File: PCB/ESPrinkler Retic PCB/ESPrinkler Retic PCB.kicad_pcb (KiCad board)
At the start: 2 copper layers, 120.4 x 85.7 mm, 138 parts, among them J4 Conn_01x19, J5 Conn_01x19, J6 Conn_01x04, Q1 AO3400A, Q10 AO3400A, Q11 AO3400A, Q2 AO3400A, Q3 AO3400A, Q4 AO3400A, Q5 AO3400A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

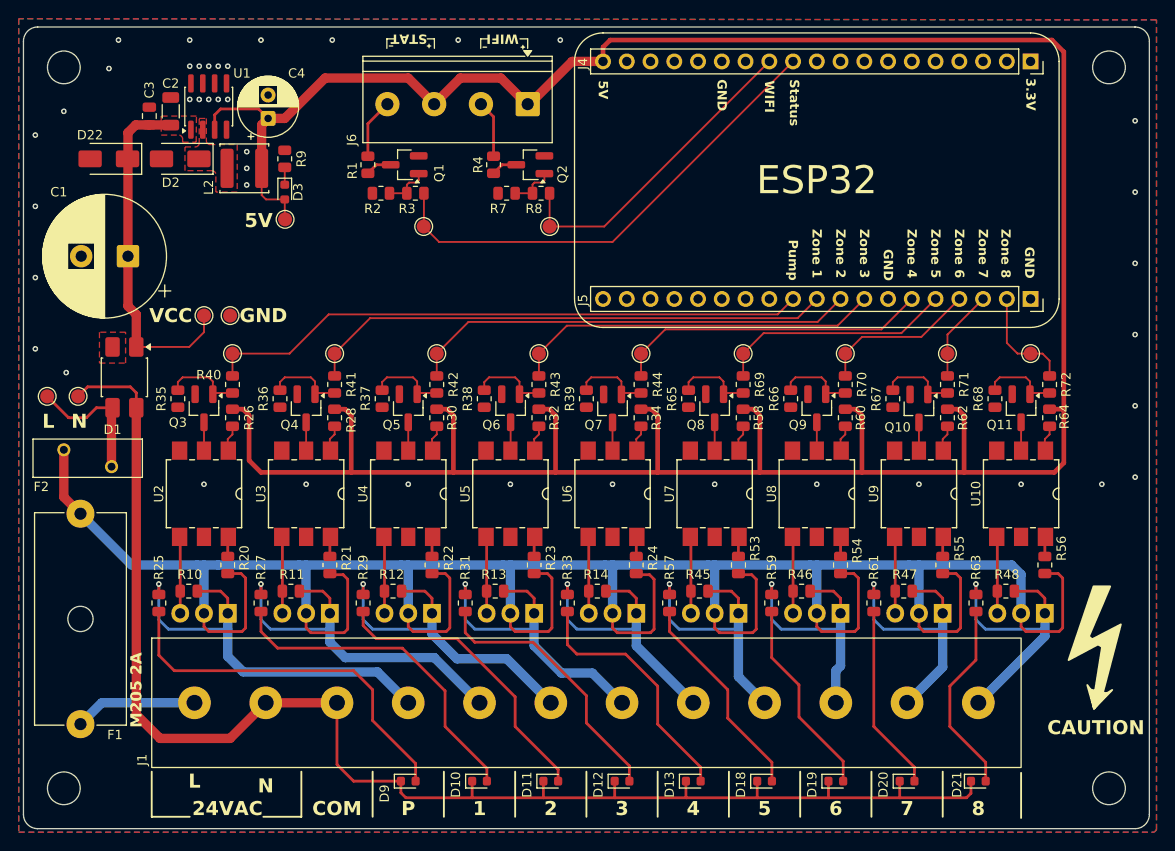
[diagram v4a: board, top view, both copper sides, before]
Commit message: Labelling as V2.0
Repo needs to change, I have been using it poorly. V2.0 will be the next "main branch". After that, forks will be used instead

Also in this commit, I have updated the custom footprints and updated the links to them in the project.
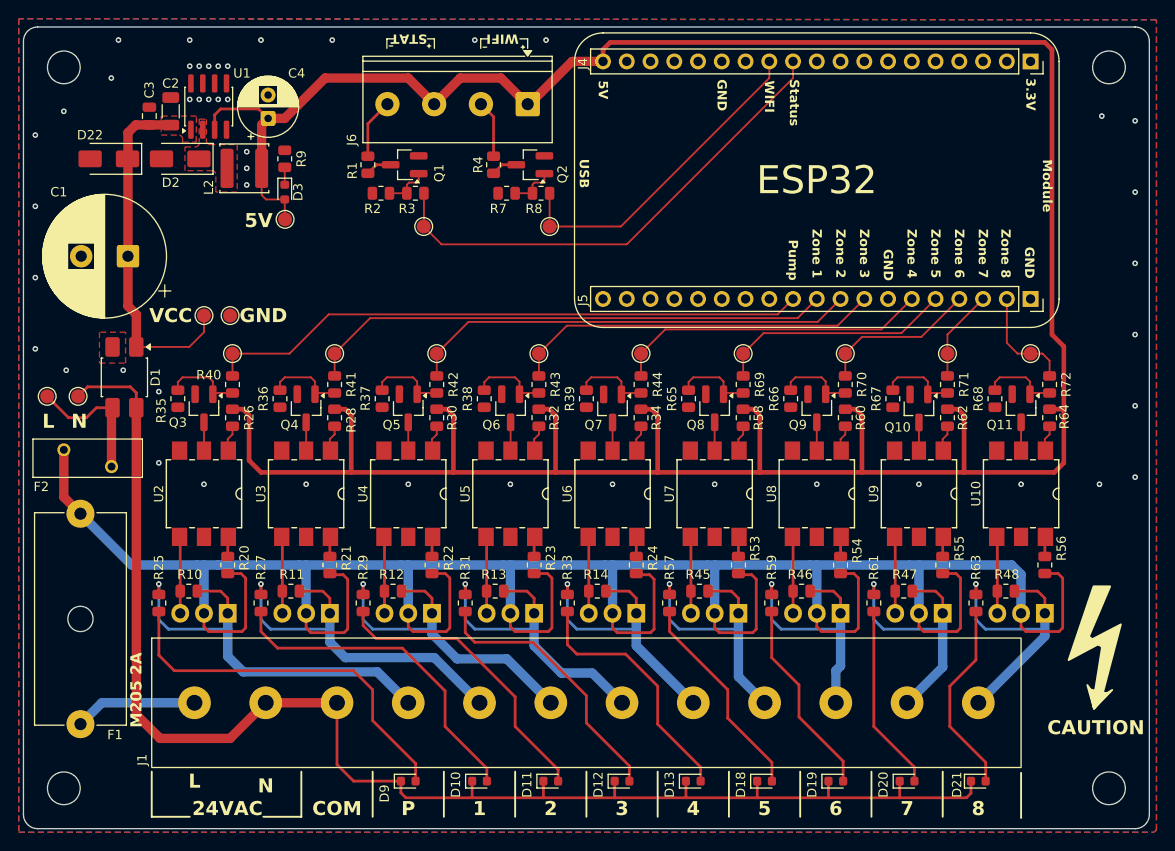
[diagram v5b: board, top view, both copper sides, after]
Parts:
- C4: value 220uF -> 180uF
- D1: footprint Package_SO:OnSemi_751EP_SOIC-4_3.9x4.725mm_P2.54mm -> Footprints:OnSemi_751EP_SOIC-4_3.9x4.725mm_P2.54mm
- D14, D15, D16, D17, D4, D5, D6, D7, D8: value Generic_Triac_A1A2G -> BTB16-600BWRG
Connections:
- net /ESP32/Pump renamed /Control Outputs/Pump Input
- net /ESP32/Status LED renamed /ESP32/Status LED CTRL
- net /ESP32/WIFI LED renamed /ESP32/WIFI LED CTRL
- net /ESP32/Zone 1 renamed /Control Outputs/Zone 1 Input
- net /ESP32/Zone 2 renamed /Control Outputs/Zone 2 Input
- net /ESP32/Zone 3 renamed /Control Outputs/Zone 3 Input
- net /ESP32/Zone 4 renamed /Control Outputs/Zone 4 Input
- net /ESP32/Zone 5 renamed /Control Outputs/Zone 5 Input
- net /ESP32/Zone 6 renamed /Control Outputs/Zone 6 Input
- net /ESP32/Zone 7 renamed /Control Outputs/Zone 7 Input
- net /ESP32/Zone 8 renamed /Control Outputs/Zone 8 Input
- net /Power & IO/To Pump renamed /Control Outputs/Pump Ouptput
- net /Power & IO/To Zone 1 renamed /Control Outputs/Zone 1 Ouptput
- net /Power & IO/To Zone 2 renamed /Control Outputs/Zone 2 Ouptput
- net /Power & IO/To Zone 3 renamed /Control Outputs/Zone 3 Ouptput
- net /Power & IO/To Zone 4 renamed /Control Outputs/Zone 4 Ouptput
- net /Power & IO/To Zone 5 renamed /Control Outputs/Zone 5 Ouptput
- net /Power & IO/To Zone 6 renamed /Control Outputs/Zone 6 Ouptput
- net /Power & IO/To Zone 7 renamed /Control Outputs/Zone 7 Ouptput
- net /Power & IO/To Zone 8 renamed /Control Outputs/Zone 8 Ouptput
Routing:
- net /ESP32/Status LED CTRL: track 51.7 -> 53.0 mm
- net +5V: track 313.4 -> 312.3 mm
- net /ESP32/WIFI LED CTRL: track 34.4 -> 35.4 mm
- net GND: vias 42 -> 46
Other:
- board text added: "Module"
- board text added: "USB"
- board text added: "VERSION: 2.0"
- board text removed: "VERSION: 1.1"

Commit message: Change 12-pin connector
Change from screw terminal barrier block to a wire-to-board screw terminal block.

Opted for a 3-pin terminal block, 4 of them due the 12-pin not being available through lcsc, to get a total of 12 when connected together. Makes the design a bit confusing but the BOM is accurate
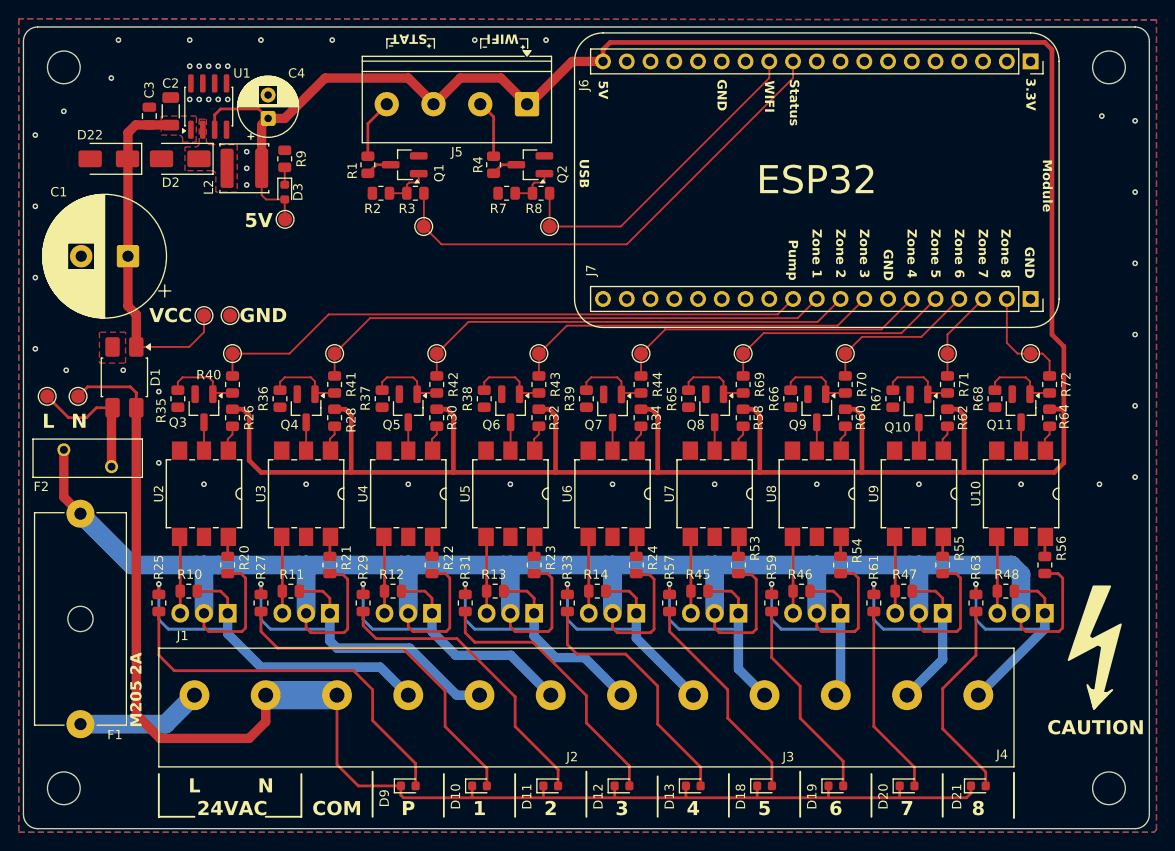
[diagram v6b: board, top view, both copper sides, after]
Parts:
- added J2: DB910-7.62-3P-GN-S, Footprints:DORABO_DB910-7.62-3P-GN-S_1x03_P7.62mm_Vertical, F.Cu at (169.7, 143.5)
- added J3: DB910-7.62-3P-GN-S, Footprints:DORABO_DB910-7.62-3P-GN-S_1x03_P7.62mm_Vertical, F.Cu at (192.5, 143.5)
- added J7: Conn_01x19, Connector_PinSocket_2.54mm:PinSocket_1x19_P2.54mm_Vertical, F.Cu at (240.0, 93.5)
- J1: value ~ -> DB910-7.62-3P-GN-S; footprint Footprints:DBT30C-7.62-12P-BK-P -> Footprints:DORABO_DB910-7.62-3P-GN-S_1x03_P7.62mm_Vertical
- J4: value Conn_01x19 -> DB910-7.62-3P-GN-S; footprint Connector_PinSocket_2.54mm:PinSocket_1x19_P2.54mm_Vertical -> Footprints:DORABO_DB910-7.62-3P-GN-S_1x03_P7.62mm_Vertical
- J5: value Conn_01x19 -> Conn_01x04; footprint Connector_PinSocket_2.54mm:PinSocket_1x19_P2.54mm_Vertical -> TerminalBlock_Phoenix:TerminalBlock_Phoenix_PT-1,5-4-5.0-H_1x04_P5.00mm_Horizontal
- J6: value Conn_01x04 -> Conn_01x19; footprint TerminalBlock_Phoenix:TerminalBlock_Phoenix_PT-1,5-4-5.0-H_1x04_P5.00mm_Horizontal -> Connector_PinSocket_2.54mm:PinSocket_1x19_P2.54mm_Vertical
- moved J4 79.3 mm to (215.4, 143.5), turned to 0 degrees
- moved J5 57.7 mm to (186.2, 72.6), turned to 180 degrees
- moved J6 54.0 mm to (240.0, 68.1), turned to -90 degrees
- moved J1 7.80 mm to (146.8, 143.5)
- moved D10 0.51 mm to (181.1, 145.5)
- moved D11 0.51 mm to (188.7, 145.5)
- moved D12 0.51 mm to (196.3, 145.5)
- moved D13 0.51 mm to (204.0, 145.5)
- moved D18 0.51 mm to (211.6, 145.5)
- moved D19 0.51 mm to (219.2, 145.5)
- moved D20 0.51 mm to (226.8, 145.5)
- moved D21 0.51 mm to (234.4, 145.5)
- moved D9 0.51 mm to (173.5, 145.5)
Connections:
- J4 pad 1: unconnected-(J4-Pin_1-Pad1) -> /Control Outputs/Zone 6 Ouptput
- J4 pad 2: unconnected-(J4-Pin_2-Pad2) -> /Control Outputs/Zone 7 Ouptput
- J4 pad 3: unconnected-(J4-Pin_3-Pad3) -> /Control Outputs/Zone 8 Ouptput
- J5 pad 1: GND -> +5V
- J5 pad 2: /Control Outputs/Zone 8 Input -> Net-(J5-Pin_2)
- J5 pad 3: /Control Outputs/Zone 7 Input -> +5V
- J5 pad 4: /Control Outputs/Zone 6 Input -> Net-(J5-Pin_4)
- J6 pad 1: +5V -> unconnected-(J6-Pin_1-Pad1)
- J6 pad 2: Net-(J6-Pin_2) -> unconnected-(J6-Pin_2-Pad2)
- J6 pad 3: +5V -> unconnected-(J6-Pin_3-Pad3)
- J6 pad 4: Net-(J6-Pin_4) -> unconnected-(J6-Pin_4-Pad4)
- R1 pad 2: Net-(J6-Pin_4) -> Net-(J5-Pin_4)
- R4 pad 2: Net-(J6-Pin_2) -> Net-(J5-Pin_2)
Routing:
- net Net-(J6-Pin_4): track 6.43 -> 0.00 mm
- net Net-(J5-Pin_4): track 0.00 -> 6.43 mm
- net Net-(J6-Pin_2): track 6.13 -> 0.00 mm
- net Net-(J5-Pin_2): track 0.00 -> 6.13 mm
- net /Control Outputs/Pump Ouptput: track 43.9 -> 42.1 mm
- net NEUT: track 156.0 -> 154.6 mm
- net /Control Outputs/Zone 3 Ouptput: track 33.3 -> 32.4 mm
- net /Control Outputs/Zone 4 Ouptput: track 30.0 -> 29.2 mm
- net /Control Outputs/Zone 7 Ouptput: track 29.0 -> 28.2 mm
- net /Control Outputs/Zone 5 Ouptput: track 28.6 -> 27.8 mm
- net /Control Outputs/Zone 8 Ouptput: track 30.4 -> 29.6 mm
- net /Control Outputs/Zone 6 Ouptput: track 27.7 -> 26.9 mm
- net Net-(D21-A): track 20.9 -> 21.5 mm

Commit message: Change mounting holes
Change mounting holes to M3.2 with exposed pads and vias. Add them to schematic for reference
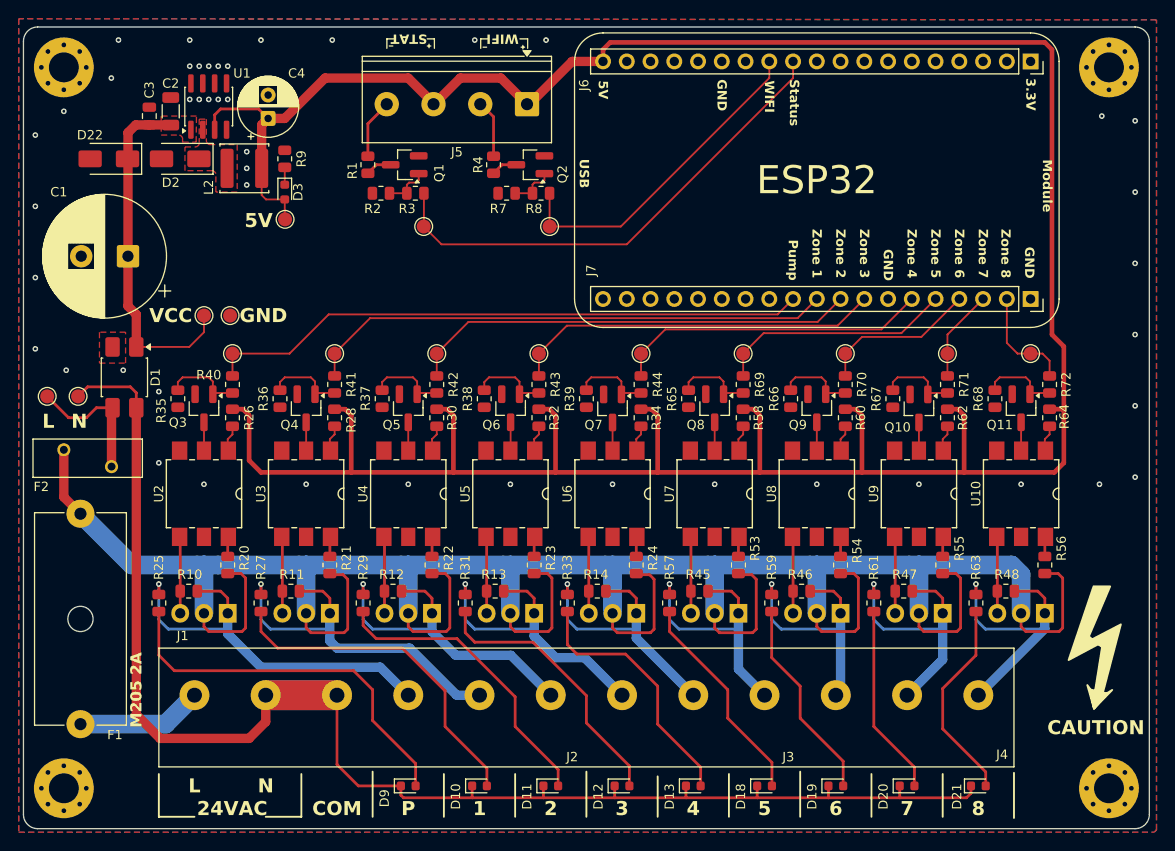
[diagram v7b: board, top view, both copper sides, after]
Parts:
- removed the REF** at (248.4, 145.8)
- removed the REF** at (248.4, 68.7)
- removed the REF** at (136.7, 68.7)
- removed the REF** at (136.7, 145.8)
- added H1: MountingHole, MountingHole:MountingHole_3.2mm_M3_Pad_Via, F.Cu at (136.7, 68.7)
- added H2: MountingHole, MountingHole:MountingHole_3.2mm_M3_Pad_Via, F.Cu at (248.4, 68.7)
- added H3: MountingHole, MountingHole:MountingHole_3.2mm_M3_Pad_Via, F.Cu at (248.4, 145.8)
- added H4: MountingHole, MountingHole:MountingHole_3.2mm_M3_Pad_Via, F.Cu at (136.7, 145.8)
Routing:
- net NEUT: track 154.6 -> 162.3 mm
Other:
- board text removed: "github.com/slippery-carrot/ESPrinkler-Retic-Controller"
